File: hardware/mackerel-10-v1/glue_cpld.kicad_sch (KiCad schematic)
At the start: 18 parts, among them J1 Conn_02x05_Odd_Even, X1 50MHz, X2 50MHz

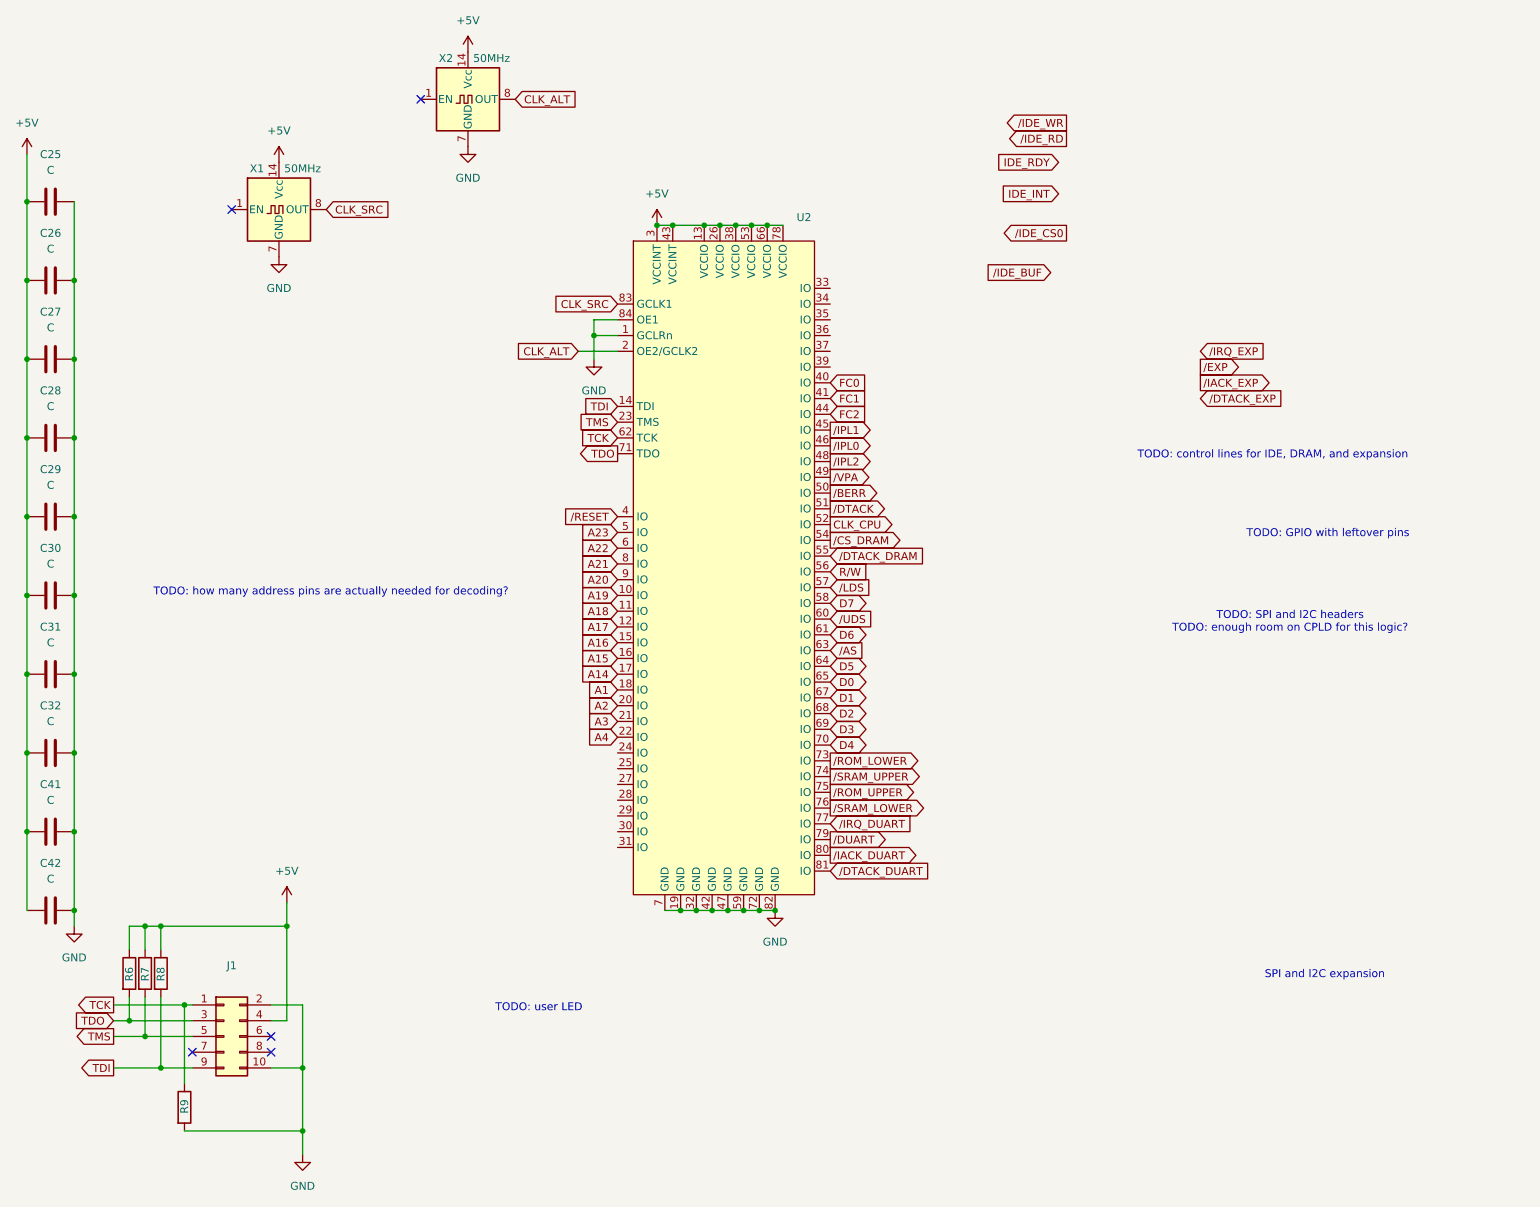
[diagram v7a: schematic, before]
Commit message: IDE interface routed
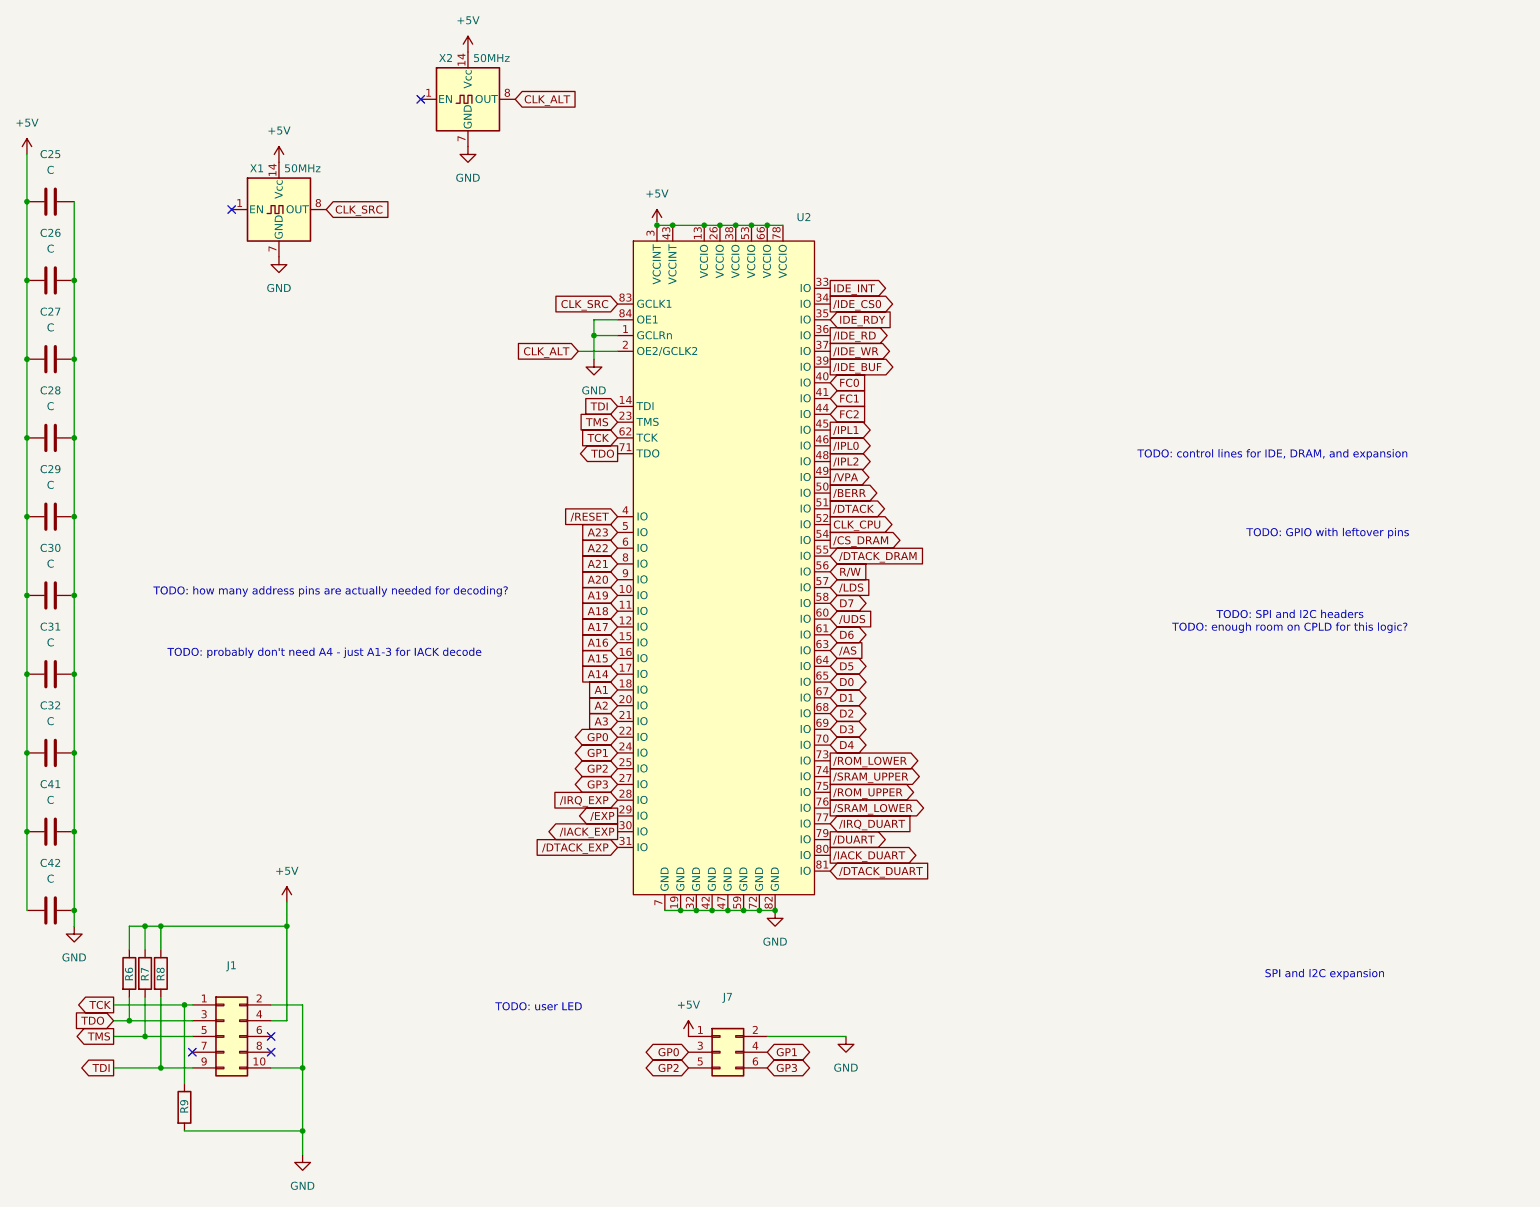
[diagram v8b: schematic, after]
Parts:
- added J7: Conn_02x03_Odd_Even, Connector_PinHeader_2.54mm:PinHeader_2x03_P2.54mm_Vertical, symbol Connector_Generic:Conn_02x03_Odd_Even
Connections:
- net +5V: now also J7.1 (Pin_1)
- net GND: now also J7.2 (Pin_2)
- net IDE_INT: now also U2.33 (IO)
- net IDE_RDY: now also U2.35 (IO)
- net /DTACK_EXP: now also U2.31 (IO)
- net /EXP: now also U2.29 (IO)
- net /IACK_EXP: now also U2.30 (IO)
- net /IDE_BUF: now also U2.39 (IO)
- net /IDE_CS0: now also U2.34 (IO)
- net /IDE_RD: now also U2.36 (IO)
- net /IDE_WR: now also U2.37 (IO)
- net /IRQ_EXP: now also U2.28 (IO)
- net GP1: now reaches U2.24 (IO)
- net GP1: now also J7.4 (Pin_4)
- net GP2: now reaches U2.25 (IO)
- net GP2: now also J7.5 (Pin_5)
- net GP3: now reaches U2.27 (IO)
- net GP3: now also J7.6 (Pin_6)
- net A4 renamed GP0
- net GP0: now also J7.3 (Pin_3)
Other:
- note added: "TODO: probably don't need A4 - just A1-3 for IACK decode"
